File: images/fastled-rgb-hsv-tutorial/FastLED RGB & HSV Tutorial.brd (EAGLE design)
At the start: 50.2 x 50.2 mm, 13 parts

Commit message: Updated PCB
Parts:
- added A3: (no value), switch-omron:B3F-10XX
- added R2: 10KΩ, SparkFun-Resistors:AXIAL-0.1EZ
- moved R1 8.28 mm to (40.0, 48.3), turned to 270 degrees
- moved C1 6.03 mm to (32.7, 5.71)
- moved LED0 2.54 mm to (40.6, 43.2)
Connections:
- new net N$1: A3.1, R2.P$2
- new net S1: A3.2, U$1.A3
- net 5V: now also A3.3
- net GND: now also R2.P$1
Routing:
- net S1: track 0.00 -> 15.7 mm
- net R1: track 36.6 -> 28.8 mm
- net N$1: track 0.00 -> 6.01 mm
- net D8: track 44.8 -> 50.6 mm
- net LED1: track 13.5 -> 11.0 mm
- net 5V: track 165.2 -> 164.3 mm
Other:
- board text added: "Blue/Val Pot = A2"
- board text added: "Button = A3"
- board text added: "FastLED RGB & HSV Tutorial by Evil Genius Labs"
- board text added: "Green/Sat Pot = A1"
- board text added: "LED0 = pin 4"
- board text added: "Pro Trinket 5V"
- board text added: "Red/Hue Pot = A0"

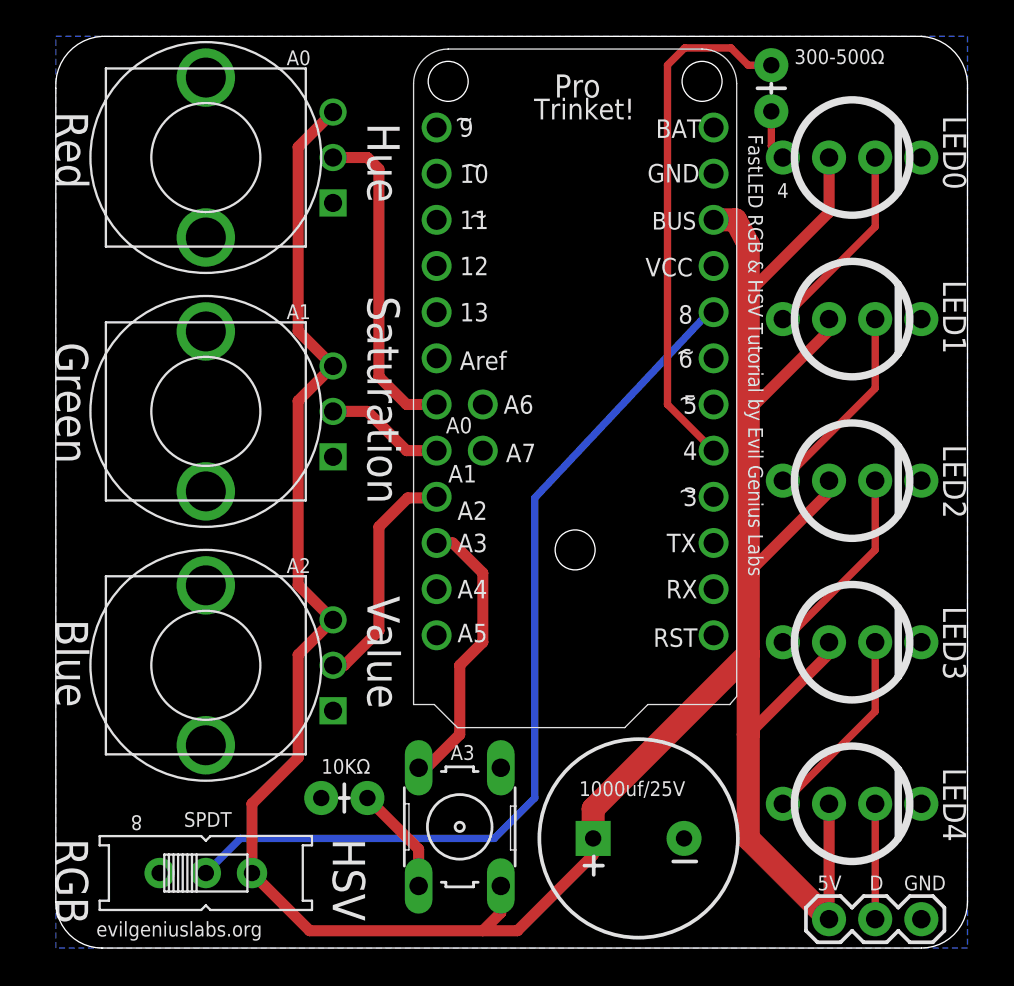
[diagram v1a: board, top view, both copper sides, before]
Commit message: Switched to 8x NeoPixel stick.
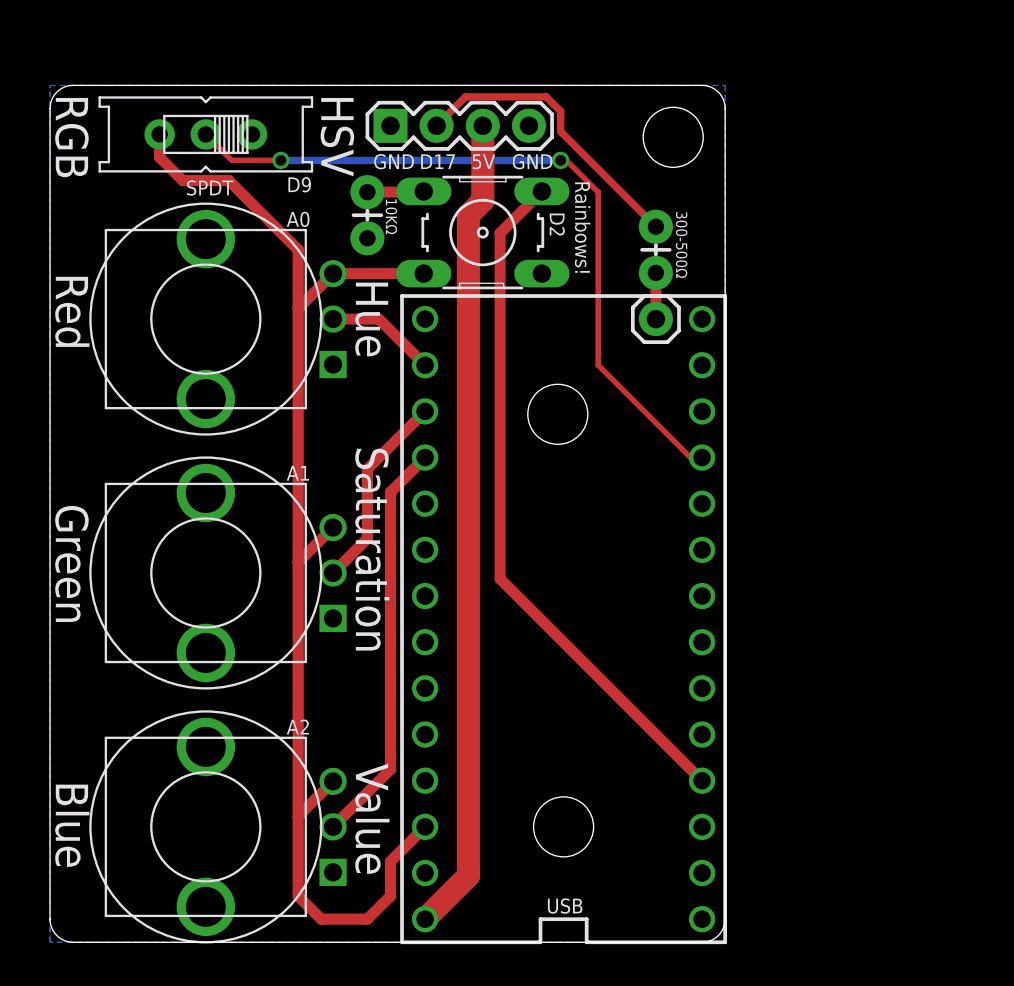
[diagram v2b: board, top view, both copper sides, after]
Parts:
- removed A3: (no value), switch-omron:B3F-10XX
- removed C1: 1000uf/25V, SparkFun-Capacitors:CPOL-RADIAL-1000UF-25V-KIT
- removed LED0, LED1, LED2, LED3, LED4: (no value), SparkFun-Connectors:1X04_NO_SILK_ALL_ROUND
- removed OUT: (no value), SparkFun-Connectors:1X03
- added D2: D2, switch-omron:B3F-10XX
- added J1: J1, SparkFun-Connectors:1X01
- added LED: (no value), SparkFun-Connectors:1X04
- added TEENSYLC: TEENSY_LC_DIL, Teensy_3_and_LC_Series_Boards_v1.1:TEENSY3-DIL
- added U$3, U$8: (no value), SparkFun-Electromechanical:STAND-OFF
- B-S-POT: value (none) -> B-S-POT
- G-S-POT: value (none) -> G-S-POT
- R-H-POT: value (none) -> R-H-POT
- SPDT: value (none) -> SPDT
- U$1: value PRO_TRINKET -> (none); device adafruit:PROTRINKET -> SparkFun-Electromechanical:STAND-OFF
- moved SPDT 40.6 mm to (8.89, 44.5), turned to 180 degrees
- moved R2 30.9 mm to (17.8, 38.7), turned to 90 degrees
- moved R1 13.1 mm to (33.7, 36.8), turned to 90 degrees
- moved B-S-POT 8.89 mm to (8.89, 6.35)
- moved G-S-POT 8.89 mm to (8.89, 20.3)
- moved R-H-POT 8.89 mm to (8.89, 34.3)
- moved U$1 7.52 mm to (28.3, 29.1)
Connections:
- removed net 5V: A3.3, B-S-POT.3, C1.+, G-S-POT.3, LED0.2, LED1.2, LED2.2, LED3.2, LED4.2, OUT.1, R-H-POT.3, SPDT.S, U$1.USB
- removed net BAT+: U$1.BAT+
- removed net D8: SPDT.P, U$1.8
- removed net LED1: LED0.3, LED1.1
- removed net LED2: LED1.3, LED2.1
- removed net LED3: LED2.3, LED3.1
- removed net LED4: LED3.3, LED4.1
- removed net LED5: LED4.3, OUT.2
- removed net VCC: U$1.VCC
- new net 3.3V: B-S-POT.3, D2.3, G-S-POT.3, R-H-POT.3, SPDT.S, TEENSYLC.3.3V
- new net B1: SPDT.P, TEENSYLC.9
- new net VIN: LED.3, TEENSYLC.VIN
- net GND: now also LED.1, LED.4, TEENSYLC.AGND, TEENSYLC.GND; no longer C1.-, LED0.4, LED1.4, LED2.4, LED3.4, LED4.4, OUT.3, U$1.GND
- net LED0: now also LED.2; no longer LED0.1
- net N$1: now also D2.1; no longer A3.1
- net P0: now also TEENSYLC.14/A0; no longer U$1.A0
- net P1: now also TEENSYLC.15/A1; no longer U$1.A1
- net P2: now also TEENSYLC.16/A2; no longer U$1.A2
- net R1: now also J1.1, TEENSYLC.17/A3; no longer U$1.4
- net S1: now also D2.2, TEENSYLC.2; no longer A3.2, U$1.A3
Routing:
- net 5V: track 164.3 -> 0.00 mm
- net 3.3V: track 0.00 -> 70.4 mm
- net D8: track 50.6 -> 0.00 mm
- net VIN: track 0.00 -> 45.0 mm
- net B1: track 0.00 -> 40.2 mm, vias 0 -> 2
- net R1: track 28.8 -> 2.54 mm
- net S1: track 15.7 -> 38.0 mm
- net LED0: track 2.80 -> 16.3 mm
- net P0: track 18.0 -> 6.12 mm
- net LED4: track 11.0 -> 0.00 mm
- net LED2: track 11.0 -> 0.00 mm
- net LED1: track 11.0 -> 0.00 mm
- net LED3: track 11.0 -> 0.00 mm
- net P2: track 12.9 -> 22.4 mm
- net LED5: track 6.35 -> 0.00 mm
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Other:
- board size 50.2 x 50.2 mm -> 37.1 x 47.1 mm
- board text added: "Blue/Val Pot"
- board text added: "Button"
- board text added: "D17"
- board text added: "D2"
- board text added: "D6"
- board text added: "D9"
- board text added: "Green/Sat Pot"
- board text added: "LED0"
- board text added: "Rainbows!"
- board text added: "Red/Hue Pot"
- board text added: "Switch"
- board text added: "Teensy LC"
- board text added: "USB"
- board text removed: "4"
- board text removed: "8"
- board text removed: "Blue/Val Pot = A2"
- board text removed: "Button = A3"
- board text removed: "D"
- board text removed: "FastLED RGB & HSV Tutorial by Evil Genius Labs"
- board text removed: "Green/Sat Pot = A1"
- board text removed: "LED0 = pin 4"
- board text removed: "Pro Trinket 5V"
- board text removed: "Red/Hue Pot = A0"

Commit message: Added 10uF capacitor, reworked layout.
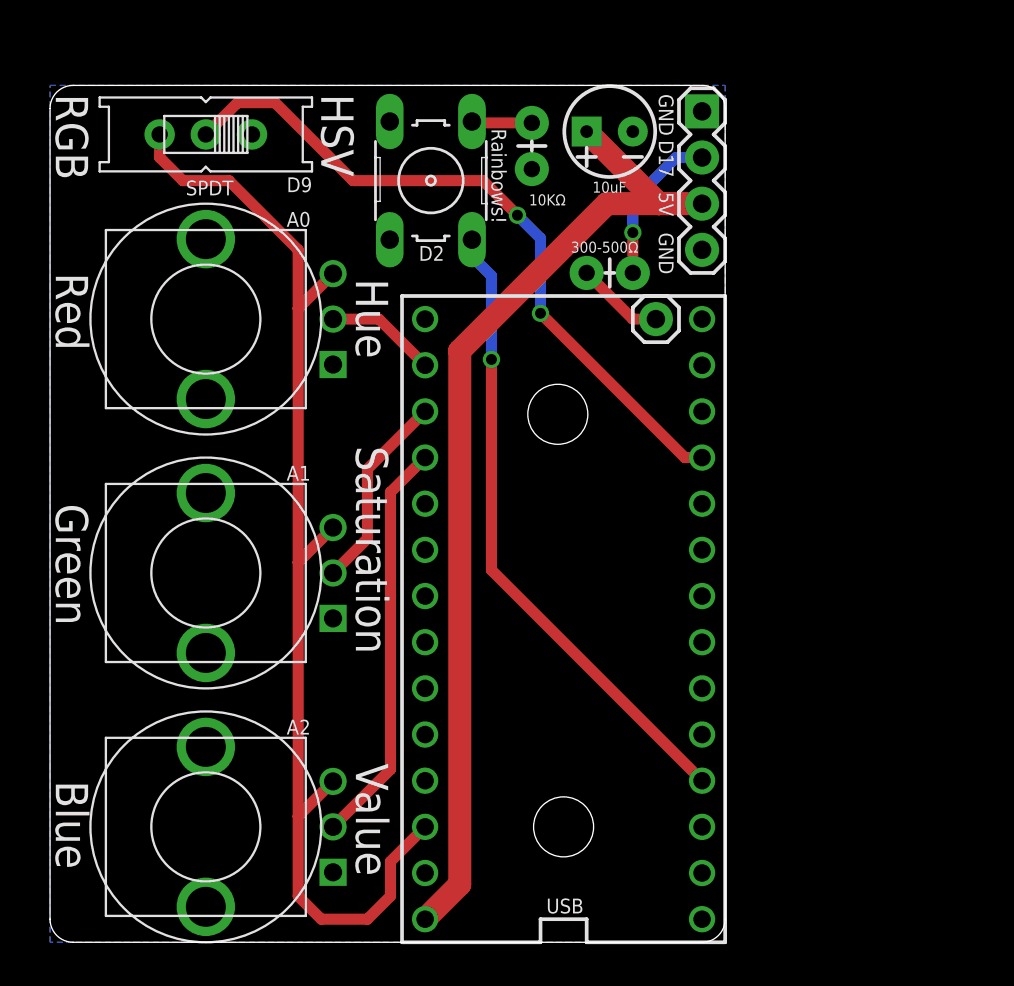
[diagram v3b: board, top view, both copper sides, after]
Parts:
- removed U$8: (no value), SparkFun-Electromechanical:STAND-OFF
- added C1: 10uF, SparkFun-Capacitors:CPOL-RADIAL-10UF-25V-KIT
- moved LED 17.2 mm to (36.2, 45.7), turned to 270 degrees
- moved R2 9.82 mm to (26.8, 42.5)
- moved D2 4.04 mm to (21.3, 41.9), turned to 270 degrees
- moved R1 3.81 mm to (29.8, 36.8), turned to 0 degrees
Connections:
- net GND: now also C1.2
- net VIN: now also C1.1
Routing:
- net VIN: track 45.0 -> 54.4 mm
- net LED0: track 16.3 -> 8.77 mm, vias 0 -> 1
- net 3.3V: track 70.4 -> 65.4 mm
- net S1: track 38.0 -> 35.0 mm, vias 0 -> 1
- net R1: track 2.54 -> 4.86 mm
- net B1: track 40.2 -> 38.5 mm

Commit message: Updated site
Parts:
- removed J1: J1, SparkFun-Connectors:1X01
- added J6: (no value), SparkFun-Connectors:1X05
- moved R1 2.54 mm to (32.4, 36.8), turned to 180 degrees
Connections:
- net GND: now also J6.3
- net R1: now also J6.1; no longer J1.1
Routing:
- net 3.3V: track 65.4 -> 79.1 mm
- net VIN: track 54.4 -> 56.4 mm
- net R1: track 4.86 -> 3.07 mm
- net LED0: track 8.77 -> 10.3 mm, vias 1 -> 2
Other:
- board text added: "v0.1 2017"
- board text removed: "D6"
